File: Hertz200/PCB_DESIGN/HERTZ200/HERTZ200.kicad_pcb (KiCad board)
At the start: 4 copper layers, 72.3 x 61.5 mm, 118 parts, among them IC1 BD33HC5MEFJ-ME2, IC2 TMP451HQDQWTQ1, IC3 BQ29701DSET, J1 SMA_CONNECTOR, J2 503960-0696, J3 SMA_CONNECTOR, J5 105164-0001, J6 GPIO_PINS, J7 SWD_PINS, J8 USB4125-GF-A-0190_REVA2, Q2 BC847-T, U1 STM32L431CCUx, U2 SIM7020E, U3 TXB0104PW, U4 SIM68M, U5 CSD16406Q3, U6 MP2636GR-P, U7 100uF, U8 100uF, U9 CSD16406Q3

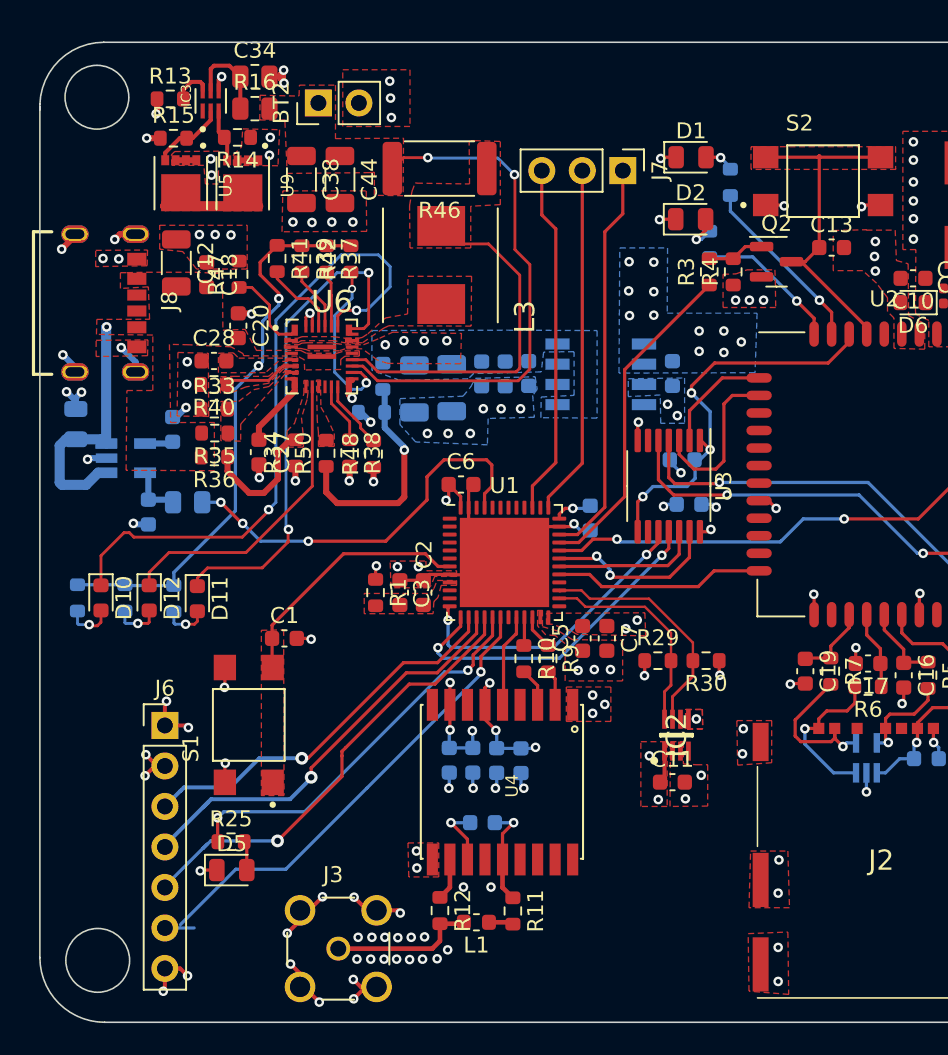
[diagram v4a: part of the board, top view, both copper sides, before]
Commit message: Finished Schematics Review
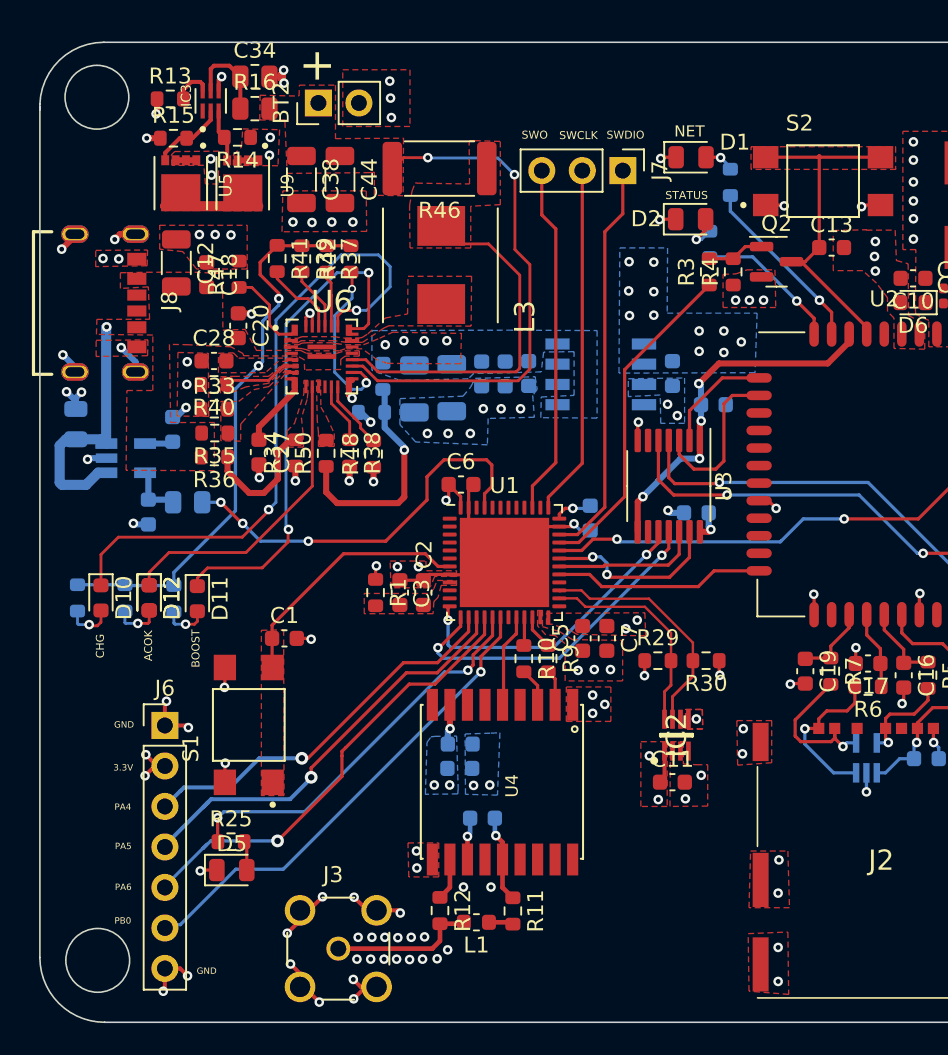
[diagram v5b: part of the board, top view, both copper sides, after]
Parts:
- removed C23: 4.7uF, Capacitor_SMD:C_0603_1608Metric
- removed C25: 0.1uF, Capacitor_SMD:C_0603_1608Metric
- added D12: BLUE_LED, LED_SMD:LED_0603_1608Metric, F.Cu at (37.5, 62.1)
- moved C14 3.97 mm to (72.8, 50.0), turned to 0 degrees
- moved C24 1.29 mm to (57.0, 71.3), turned to 0 degrees
- moved C22 0.83 mm to (56.9, 72.8), turned to 0 degrees
- moved C15 0.70 mm to (71.8, 56.8)
- moved C26 0.28 mm to (58.4, 75.9)
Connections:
- U1 pad 25: /STM32L431_MCU/DRDY -> unconnected-(U1-Pad25)
- U4 pad 6: +3V3 -> unconnected-(U4-Pad6)
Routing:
- net +3V3: track 28.5 -> 17.4 mm, vias 36 -> 32
- net GND: track 122.0 -> 115.5 mm, vias 170 -> 167
- net /SIM7020E/VDD_EXT: track 25.4 -> 22.7 mm, vias 3 -> 4
- net Net-(C26-Pad2): track 6.45 -> 5.18 mm
- net /STM32L431_MCU/GPIO05: track 31.3 -> 30.4 mm
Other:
- board text added: "+"
- board text added: "3.3V"
- board text added: "ACOK"
- board text added: "BOOST"
- board text added: "CHG"
- board text added: "COMPANY : WIGXEL CORP"
- board text added: "DESIGNER : JOSEPH OGBONNA"
- board text added: "GND"
- board text added: "NET"
- board text added: "PA4"
- board text added: "PA5"
- board text added: "PA6"
- board text added: "PB0"
- board text added: "STATUS"
- board text added: "SWCLK"
- board text added: "SWDIO"
- board text added: "SWO"

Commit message: BOM
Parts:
- removed J6: GPIO_PINS, Connector_PinHeader_2.54mm:PinHeader_1x07_P2.54mm_Vertical
- removed R41: 10K, Resistor_SMD:R_0603_1608Metric
- removed U5, U9: CSD16406Q3, CSD16406Q3:TRANS_CSD16406Q3
- added J4: GPIO_PINS, Connector_PinHeader_2.54mm:PinHeader_1x06_P2.54mm_Vertical, F.Cu at (34.1, 66.6)
- added Q1: CSD16301Q2, Package_SON:Texas_DQK, F.Cu at (41.2, 36.1)
- added Q3: CSD16301Q2, Package_SON:Texas_DQK, F.Cu at (37.4, 36.1)
- C20, C48: value 1uF -> 0.1uF
- moved D6 13.2 mm to (91.1, 31.7), turned to 0 degrees
- moved J7 4.06 mm to (67.2, 31.2)
- moved C10 1.14 mm to (85.3, 43.2)
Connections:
- net /MP2636/COUT renamed Net-(IC3-Pad2)
- net /MP2636/DOUT renamed Net-(IC3-Pad3)
- U6 pad 26: Net-(R41-Pad2) -> GND
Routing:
- net Net-(Q1-Pad1): track 0.00 -> 10.2 mm
- net Net-(U5-Pad5): track 5.84 -> 0.00 mm
- net /STM32L431_MCU/SWDIO: track 24.3 -> 29.2 mm
- net /STM32L431_MCU/SWCLK: track 21.1 -> 26.1 mm
- net /STM32L431_MCU/SWO: track 21.2 -> 26.1 mm
- net Net-(R41-Pad2): track 4.92 -> 0.00 mm
- net /STM32L431_MCU/GPIO01: track 24.5 -> 27.5 mm
- net /STM32L431_MCU/GPIO03: track 29.0 -> 32.1 mm
- net /STM32L431_MCU/GPIO05: track 30.4 -> 33.3 mm
- net /STM32L431_MCU/GPIO02: track 27.0 -> 29.7 mm
- net GND: track 115.5 -> 113.0 mm, vias 167 -> 168
- net Net-(IC3-Pad3): track 3.31 -> 4.23 mm
- net Net-(IC3-Pad2): track 4.74 -> 5.60 mm
- added copper zone on F.Cu, net Net-(Q1-Pad1)

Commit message: update
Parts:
- removed D6: ESD, Diode_SMD:D_0603_1608Metric
- removed R1: 0R, Resistor_SMD:R_0603_1608Metric
- added C49: 27pF, Capacitor_SMD:C_0603_1608Metric, F.Cu at (48.0, 59.3)
- added C50: 27pF, Capacitor_SMD:C_0603_1608Metric, F.Cu at (50.9, 64.9)
- added FB1: MPZ1608S471ATA00, Inductor_SMD:L_0603_1608Metric, B.Cu at (50.1, 63.0)
- added R52: 10K, Resistor_SMD:R_0603_1608Metric, F.Cu at (60.3, 53.8)
- added Y1: ABM3B, ABM3B-8:XTAL_ABM3B-8.000MHZ-B2-T, F.Cu at (50.8, 60.9)
- C2, C3: moved to B.Cu
- R14, R15: footprint Resistor_SMD:R_0603_1608Metric -> Resistor_SMD:R_0805_2012Metric
- moved C13 3.20 mm to (81.9, 42.9)
- moved C10 3.19 mm to (87.9, 41.4), turned to 0 degrees
- moved C2 1.98 mm to (53.1, 63.0)
- moved C3 1.98 mm to (51.6, 63.0)
- moved U8 1.57 mm to (91.7, 38.6)
- moved U7 1.16 mm to (91.6, 33.7)
- moved C26 0.25 mm to (58.4, 75.7)
- moved R14 0.18 mm to (43.0, 33.4)
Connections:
- U1 pad 28: SIM7020E_RST -> unconnected-(U1-Pad28)
- U1 pad 40: PMIC_INT -> unconnected-(U1-Pad40)
- U1 pad 41: PMIC_CE -> unconnected-(U1-Pad41)
- U1 pad 42: PMIC_SCL -> unconnected-(U1-Pad42)
- U1 pad 43: PMIC_SDA -> unconnected-(U1-Pad43)
- U1 pad 44: unconnected-(U1-Pad44) -> Net-(U1-Pad44)
- U1 pad 5: unconnected-(U1-Pad5) -> Net-(U1-Pad5)
- U1 pad 6: unconnected-(U1-Pad6) -> Net-(U1-Pad6)
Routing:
- net GND: track 113.0 -> 129.5 mm, vias 168 -> 170
- net Net-(U1-Pad5): track 0.00 -> 9.76 mm
- net Net-(U1-Pad6): track 0.00 -> 8.49 mm
- net /STM32L431_MCU/VDDA: track 0.00 -> 7.80 mm, vias 0 -> 1
- net /STM32L431_MCU/NRST: track 16.1 -> 20.6 mm
- net Net-(U1-Pad44): track 0.00 -> 2.52 mm
- net /MP2636/VCC: track 35.8 -> 34.4 mm
- net Net-(R49-Pad2): track 14.3 -> 13.2 mm
- net /STM32L431_MCU/GPIO03: track 32.1 -> 31.1 mm
- net +3V3: track 17.5 -> 18.2 mm
- net Net-(C26-Pad2): track 5.18 -> 5.71 mm
- net /MP2636/VIN: vias 1 -> 2
- removed copper zone on F.Cu, net /STM32L431_MCU/VDDA
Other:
- board text added: "."
